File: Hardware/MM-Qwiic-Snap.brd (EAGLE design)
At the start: 67.3 x 58.4 mm, 44 parts, among them J15 MICROMOD-2222-C, J2 QWIIC_RIGHT_ANGLE, U5 AP7361C-33FGEUDFN-8

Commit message: Preliminary schematic done?
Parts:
- added C3, C4: 4.7uF, SparkFun-Capacitors:0603
- added D3: 3A/10V/280mV, SparkFun-DiscreteSemi:SOD-323
- added D4: Yellow, SparkFun-LED:LED-0603
- added JP1: JUMPER-SMT_2_NC_TRACE_SILK, SparkFun-Jumpers:SMT-JUMPER_2_NC_TRACE_SILK
- added R1: 2.2k, SparkFun-Resistors:0603
- added R4: 1k, SparkFun-Resistors:0603
- added U1: MCP73831, SparkFun-IC-Power:SOT23-5
- moved C11 81.3 mm to (-0.85, -138.4)
- moved C10 69.7 mm to (-0.85, -125.7)
- moved C9 59.2 mm to (-0.85, -113.0)
- moved C1 47.6 mm to (-0.85, -100.3)
- moved C13 31.1 mm to (-0.85, -87.6)
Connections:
- new net 5V: C4.1, D3.C, D4.A, JP1.2, U1.4
- new net N$2: R1.2, U1.5
- new net N$3: R4.1, U1.1
- new net N$5: C3.1, D3.A, J3.2, U1.3
- new net N$8: D4.C, R4.2
- net GND: now also C3.2, C4.2, J3.1, R1.1, U1.2
- net VIN: now also JP1.1

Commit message: Board layout
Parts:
- moved R4 180.2 mm to (17.8, 17.8), turned to 270 degrees
- moved JP1 179.6 mm to (15.2, 17.8), flipped to the bottom
- moved D3 176.9 mm to (15.2, 22.9)
- moved D4 173.7 mm to (16.5, 15.2)
- moved C3 170.0 mm to (17.8, 22.9), turned to 90 degrees
- moved C4 168.2 mm to (15.2, 17.8)
- moved C11 147.4 mm to (11.4, 8.47), turned to 270 degrees
- moved C10 134.7 mm to (10.2, 8.47), turned to 270 degrees
- moved C9 121.9 mm to (8.89, 8.47), turned to 270 degrees
- moved C1 117.4 mm to (10.6, 16.5)
- moved C13 106.0 mm to (10.6, 17.8)
- moved R1 101.7 mm to (12.7, 20.3), turned to 270 degrees
- moved U1 96.7 mm to (15.2, 20.3), turned to 90 degrees
- moved BYP 94.6 mm to (3.81, 21.6), flipped to the bottom, turned to 180 degrees
- moved F2 90.3 mm to (3.81, 21.6)
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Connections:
- net 3.3V_EN: now also J15.4
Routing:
- net V_USB: track 0.00 -> 18.9 mm, vias 0 -> 1
- net N$5: track 0.00 -> 12.1 mm
- net VIN: track 0.00 -> 10.7 mm
- net 3.3V: track 0.00 -> 9.96 mm
- net N$1: track 0.00 -> 7.91 mm
- net 5V: track 0.00 -> 7.60 mm, vias 0 -> 1
- net GND: track 0.00 -> 5.90 mm
- net USB_D-: track 0.00 -> 2.58 mm
- net N$4: track 0.00 -> 2.44 mm, vias 0 -> 1
- net USB_D+: track 0.00 -> 2.41 mm
- net N$3: track 0.00 -> 1.87 mm
- net N$8: track 0.00 -> 1.85 mm
- net N$10: track 0.00 -> 1.79 mm
- net N$11: track 0.00 -> 1.63 mm
- net N$2: track 0.00 -> 1.28 mm
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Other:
- board size 67.3 x 58.4 mm -> 78.7 x 34.3 mm

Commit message: Layout
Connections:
- net VIN: now also J15.9
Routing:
- net 3.3V: track 9.96 -> 72.0 mm, vias 0 -> 2
- net VIN: track 10.7 -> 39.8 mm, vias 0 -> 2
- net I2C_SDA: track 0.00 -> 20.2 mm, vias 0 -> 2
- net I2C_SCL: track 0.00 -> 19.6 mm, vias 0 -> 2
- net !RESET!: track 0.00 -> 18.9 mm, vias 0 -> 2
- net 3.3V_EN: track 0.00 -> 17.6 mm, vias 0 -> 1
- net USB_D-: track 2.58 -> 18.9 mm, vias 0 -> 2
- net USB_D+: track 2.41 -> 17.7 mm, vias 0 -> 2
- net !BOOT!: track 0.00 -> 13.9 mm
- net VREG_EN: track 0.00 -> 6.73 mm, vias 0 -> 1
- net 5V: track 7.60 -> 12.0 mm
- net N$1: track 7.91 -> 9.27 mm
- net V_USB: track 18.9 -> 18.3 mm
- net GND: vias 0 -> 10

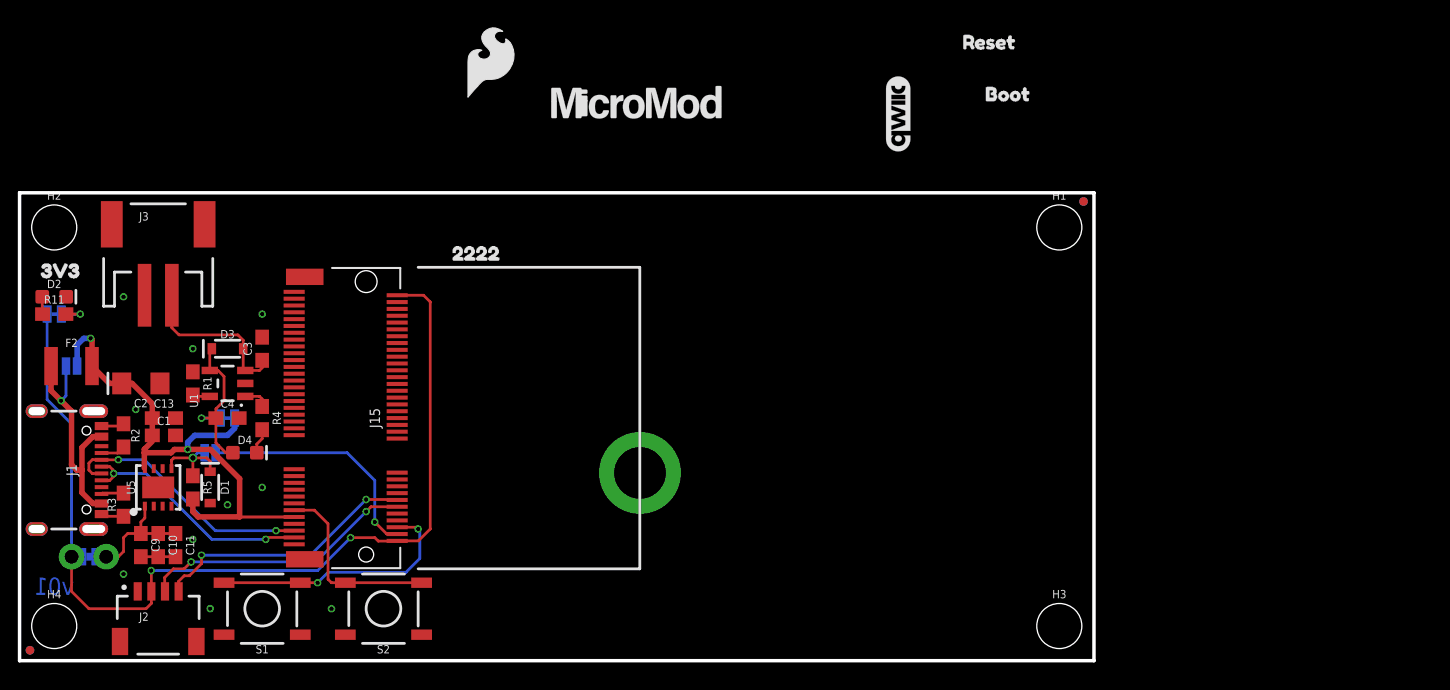
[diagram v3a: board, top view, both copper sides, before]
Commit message: Created part for stand off, proto layout finished
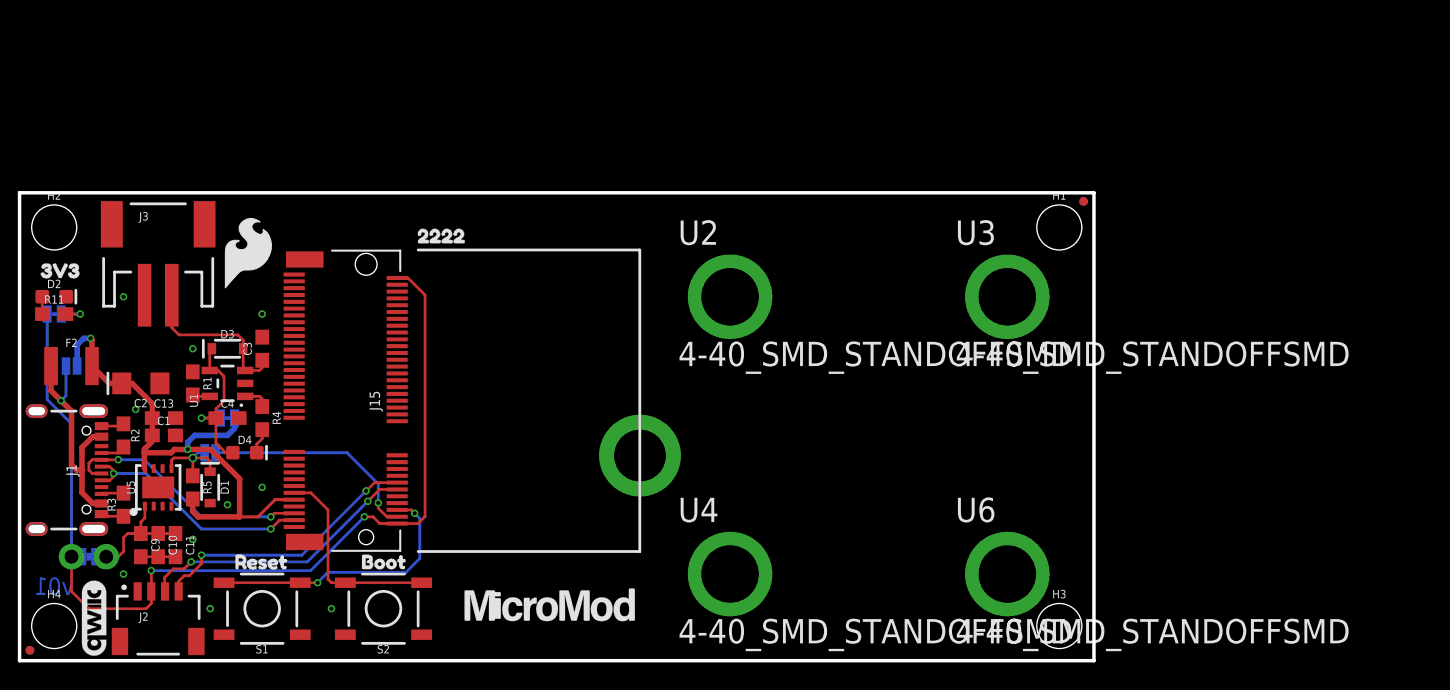
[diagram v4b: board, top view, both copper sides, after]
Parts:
- added U2, U3, U4, U6: 4-40_SMD_STANDOFFSMD, qwiic_carrier:4-40_1/8_SMD_STANDOFF
- moved LOGO2 69.6 mm to (5.46, 3.11)
- moved U$2 65.5 mm to (14.9, 7.24)
- moved U$19 57.1 mm to (24.1, 7.24)
- moved LOGO3 47.7 mm to (24.0, 9.65)
- moved U$68 47.7 mm to (24.1, 15.2)
- moved LOGO1 45.8 mm to (24.1, 19.1)
- moved U$67 37.4 mm to (38.9, 4.06)
- moved U$44 22.6 mm to (16.8, 29.8)
- moved U$55 2.84 mm to (28.2, 31.1)
- moved H5 1.27 mm to (45.5, 15.0)
- moved J15 1.27 mm to (25.4, 19.1)
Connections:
- net GND: now also U2.1, U3.1, U4.1, U6.1
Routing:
- net 3.3V_EN: track 17.6 -> 16.3 mm
- net !BOOT!: track 13.9 -> 15.0 mm
- net !RESET!: track 18.9 -> 19.9 mm
- net I2C_SDA: track 20.2 -> 20.7 mm
- net VIN: track 39.8 -> 40.3 mm
- net I2C_SCL: track 19.6 -> 20.1 mm

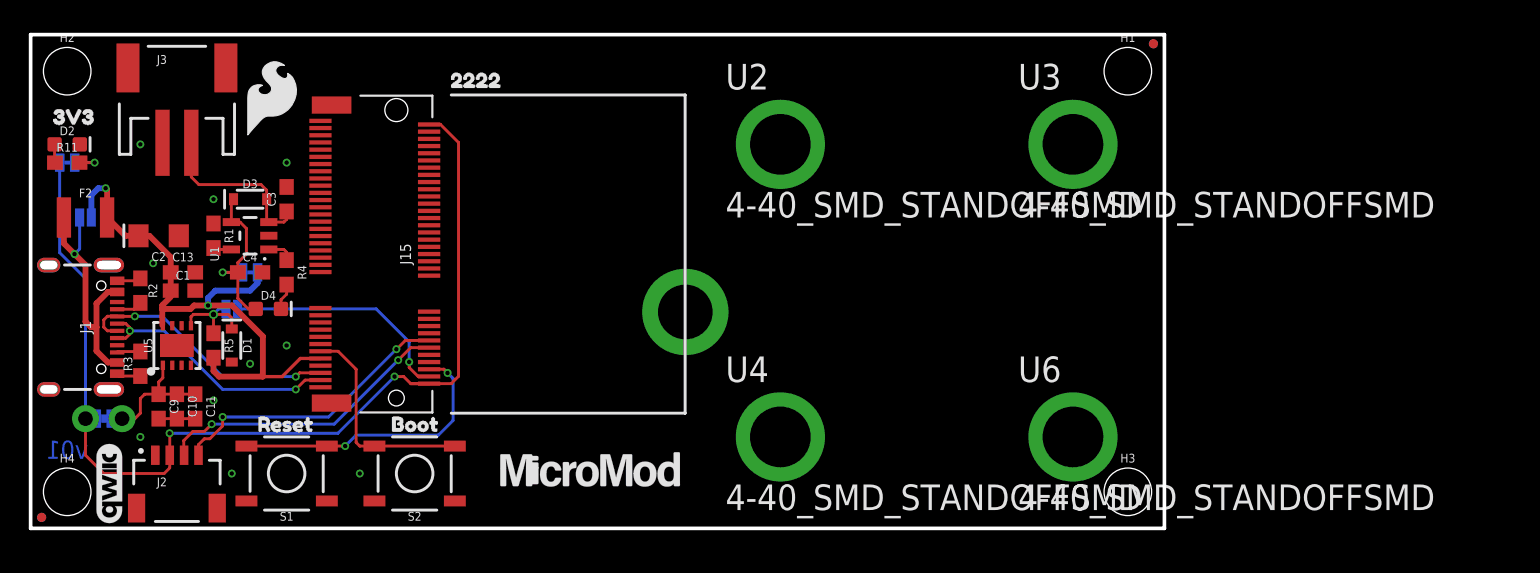
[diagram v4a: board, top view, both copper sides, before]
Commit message: Update MM-Qwiic-Snap.brd
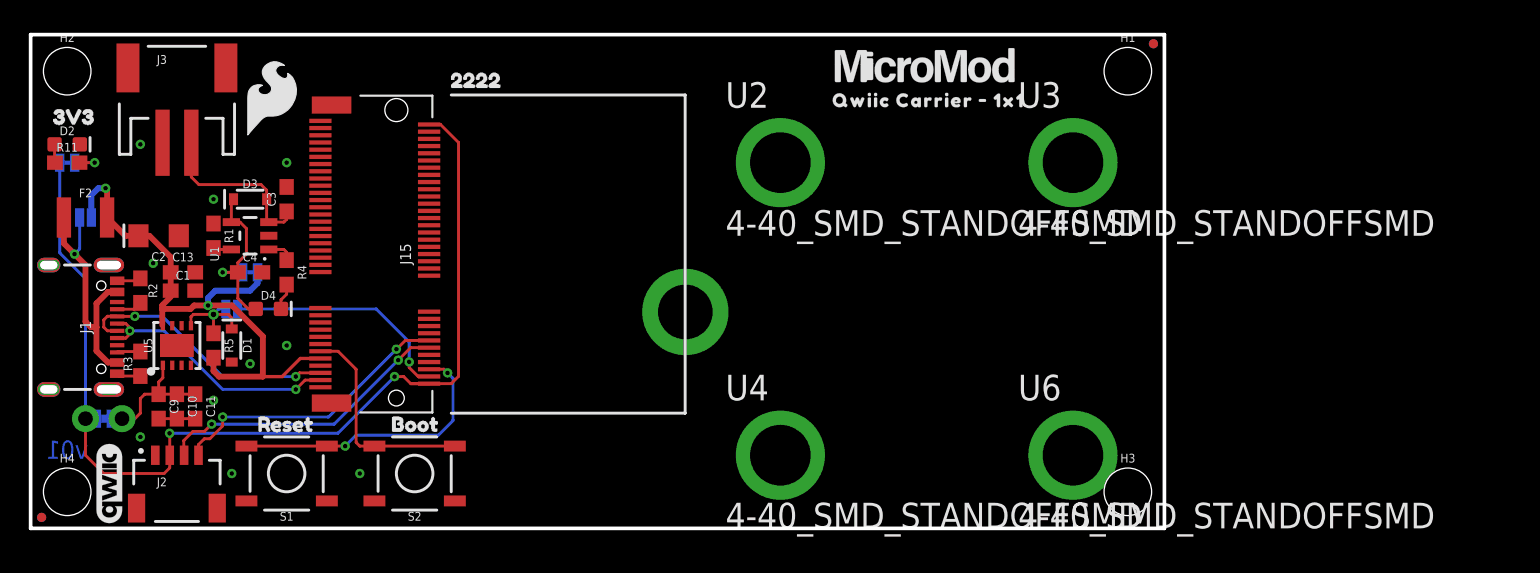
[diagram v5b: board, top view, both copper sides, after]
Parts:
- added U$3: (no value), output:QWIIC_CARRIER_#_1X1_0
- moved U$67 36.4 mm to (62.1, 32.1)
- moved U2 1.27 mm to (52.1, 25.4)
- moved U3 1.27 mm to (72.4, 25.4)
- moved U4 1.27 mm to (52.1, 5.08)
- moved U6 1.27 mm to (72.4, 5.08)
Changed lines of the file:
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@@
 <?xml version="1.0" encoding="utf-8"?>
 <!DOCTYPE eagle SYSTEM "eagle.dtd">
-<eagle version="9.5.2">
+<eagle version="9.6.2">
 <drawing>
 <settings>
-<setting alwaysvectorfont="yes"/>
+<setting alwaysvectorfont="no"/>
 <setting verticaltext="up"/>
 </settings>
@@
 </class>
 </classes>
-<designrules name="SparkFun-2-layer-FAB-LIMIT">
+<designrules name="SparkFun-2-layer-TIGHT">
 <description language="en">&lt;b&gt;SparkFun 2 Layer Design Rule Checks - STANDARD/TIGHT/FAB-LIMIT&lt;/b&gt;
 &lt;p&gt;
@@
 <param name="mtCopper" value="0.035mm 0.035mm 0.035mm 0.035mm 0.035mm 0.035mm 0.035mm 0.035mm 0.035mm 0.035mm 0.035mm 0.035mm 0.035mm 0.035mm 0.035mm 0.035mm"/>
 <param name="mtIsolate" value="1.5mm 0.15mm 0.2mm 0.15mm 0.2mm 0.15mm 0.2mm 0.15mm 0.2mm 0.15mm 0.2mm 0.15mm 0.2mm 0.15mm 0.2mm"/>
-<param name="mdWireWire" value="4mil"/>
-<param name="mdWirePad" value="4mil"/>
-<param name="mdWireVia" value="4mil"/>
-<param name="mdPadPad" value="4mil"/>
-<param name="mdPadVia" value="4mil"/>
-<param name="mdViaVia" value="4mil"/>
-<param name="mdSmdPad" value="4mil"/>
-<param name="mdSmdVia" value="4mil"/>
-<param name="mdSmdSmd" value="4mil"/>
+<param name="mdWireWire" value="7mil"/>
+<param name="mdWirePad" value="7mil"/>
+<param name="mdWireVia" value="7mil"/>
+<param name="mdPadPad" value="7mil"/>
+<param name="mdPadVia" value="7mil"/>
+<param name="mdViaVia" value="7mil"/>
+<param name="mdSmdPad" value="7mil"/>
+<param name="mdSmdVia" value="7mil"/>
+<param name="mdSmdSmd" value="7mil"/>
 <param name="mdViaViaSameLayer" value="8mil"/>
 <param name="mnLayersViaInSmd" value="2"/>
-<param name="mdCopperDimension" value="4mil"/>
-<param name="mdDrill" value="4mil"/>
+<param name="mdCopperDimension" value="7mil"/>
+<param name="mdDrill" value="7mil"/>
 <param name="mdSmdStop" value="0mil"/>
-<param name="msWidth" value="4mil"/>
-<param name="msDrill" value="6mil"/>
+<param name="msWidth" value="7mil"/>
+<param name="msDrill" value="15mil"/>
 <param name="msMicroVia" value="9.99mm"/>
 <param name="msBlindViaRatio" value="0.5"/>
@@
 <param name="rvMicroViaOuter" value="0.25"/>
 <param name="rvMicroViaInner" value="0.25"/>
-<param name="rlMinPadTop" value="5mil"/>
+<param name="rlMinPadTop" value="7mil"/>
 <param name="rlMaxPadTop" value="20mil"/>
-<param name="rlMinPadInner" value="6mil"/>
+<param name="rlMinPadInner" value="7mil"/>
 <param name="rlMaxPadInner" value="20mil"/>
-<param name="rlMinPadBottom" value="5mil"/>
+<param name="rlMinPadBottom" value="7mil"/>
 <param name="rlMaxPadBottom" value="20mil"/>
-<param name="rlMinViaOuter" value="5mil"/>
+<param name="rlMinViaOuter" value="7mil"/>
 <param name="rlMaxViaOuter" value="20mil"/>
-<param name="rlMinViaInner" value="6mil"/>
+<param name="rlMinViaInner" value="7mil"/>
 <param name="rlMaxViaInner" value="20mil"/>
 <param name="rlMinMicroViaOuter" value="4mil"/>
@@
 <element name="U$1" library="buzzard_labels (5)" package="3V31" value="" x="0.635" y="28.575" smashed="yes"/>
 <element name="U$44" library="SparkFun-Aesthetics" package="SFE_LOGO_FLAME_.2" value="" x="16.764" y="29.845" smashed="yes"/>
-<element name="U$67" library="SparkFun-MicroMod" package="MICROMOD_LOGO_.5" value="" x="38.862" y="4.064" smashed="yes"/>
+<element name="U$67" library="SparkFun-MicroMod" package="MICROMOD_LOGO_.5" value="" x="62.103" y="32.131" smashed="yes"/>
 <element name="U$68" library="SparkFun-MicroMod" package="MICROMOD_LOGO_.5" value="" x="24.13" y="15.24" smashed="yes" rot="MR0"/>
 <element name="J2" library="SparkFun-Connectors" package="JST04_1MM_RA" value="QWIIC_RIGHT_ANGLE" x="10.16" y="5.08" smashed="yes">
@@
 <attribute name="VALUE" x="15.24" y="16.637" size="0.6096" layer="28" font="vector" ratio="20" rot="MR0" align="top-center"/>
 </element>
-<element name="U2" library="qwiic_carrier" package="4-40_1/8_SMD_STANDOFF" value="4-40_SMD_STANDOFFSMD" x="52.07" y="26.67" smashed="yes">
-<attribute name="NAME" x="48.26" y="30.48" size="1.778" layer="25"/>
-<attribute name="VALUE" x="48.26" y="21.59" size="1.778" layer="25"/>
-</element>
-<element name="U3" library="qwiic_carrier" package="4-40_1/8_SMD_STANDOFF" value="4-40_SMD_STANDOFFSMD" x="72.39" y="26.67" smashed="yes">
-<attribute name="NAME" x="68.58" y="30.48" size="1.778" layer="25"/>
-<attribute name="VALUE" x="68.58" y="21.59" size="1.778" layer="25"/>
-</element>
-<element name="U4" library="qwiic_carrier" package="4-40_1/8_SMD_STANDOFF" value="4-40_SMD_STANDOFFSMD" x="52.07" y="6.35" smashed="yes">
-<attribute name="NAME" x="48.26" y="10.16" size="1.778" layer="25"/>
-<attribute name="VALUE" x="48.26" y="1.27" size="1.778" layer="25"/>
-</element>
-<element name="U6" library="qwiic_carrier" package="4-40_1/8_SMD_STANDOFF" value="4-40_SMD_STANDOFFSMD" x="72.39" y="6.35" smashed="yes">
-<attribute name="NAME" x="68.58" y="10.16" size="1.778" layer="25"/>
-<attribute name="VALUE" x="68.58" y="1.27" size="1.778" layer="25"/>
-</element>
+<element name="U2" library="qwiic_carrier" package="4-40_1/8_SMD_STANDOFF" value="4-40_SMD_STANDOFFSMD" x="52.07" y="25.4" smashed="yes">
+<attribute name="NAME" x="48.26" y="29.21" size="1.778" layer="25"/>
+<attribute name="VALUE" x="48.26" y="20.32" size="1.778" layer="25"/>
+</element>
+<element name="U3" library="qwiic_carrier" package="4-40_1/8_SMD_STANDOFF" value="4-40_SMD_STANDOFFSMD" x="72.39" y="25.4" smashed="yes">
+<attribute name="NAME" x="68.58" y="29.21" size="1.778" layer="25"/>
+<attribute name="VALUE" x="68.58" y="20.32" size="1.778" layer="25"/>
+</element>
+<element name="U4" library="qwiic_carrier" package="4-40_1/8_SMD_STANDOFF" value="4-40_SMD_STANDOFFSMD" x="52.07" y="5.08" smashed="yes">
+<attribute name="NAME" x="48.26" y="8.89" size="1.778" layer="25"/>
+<attribute name="VALUE" x="48.26" y="0" size="1.778" layer="25"/>
+</element>
+<element name="U6" library="qwiic_carrier" package="4-40_1/8_SMD_STANDOFF" value="4-40_SMD_STANDOFFSMD" x="72.39" y="5.08" smashed="yes">
+<attribute name="NAME" x="68.58" y="8.89" size="1.778" layer="25"/>
+<attribute name="VALUE" x="68.58" y="0" size="1.778" layer="25"/>
+</element>
+<element name="U$3" library="output" package="QWIIC_CARRIER_#_1X1_0" value="" x="54.991" y="29.718" smashed="yes"/>
 </elements>
 <signals>
@@
 <mfgpreviewcolor name="substratecolor" color="0xFF786E46"/>
 </mfgpreviewcolors>
+<errors>
+</errors>
 </board>
 </drawing>

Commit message: Switch out stand offs
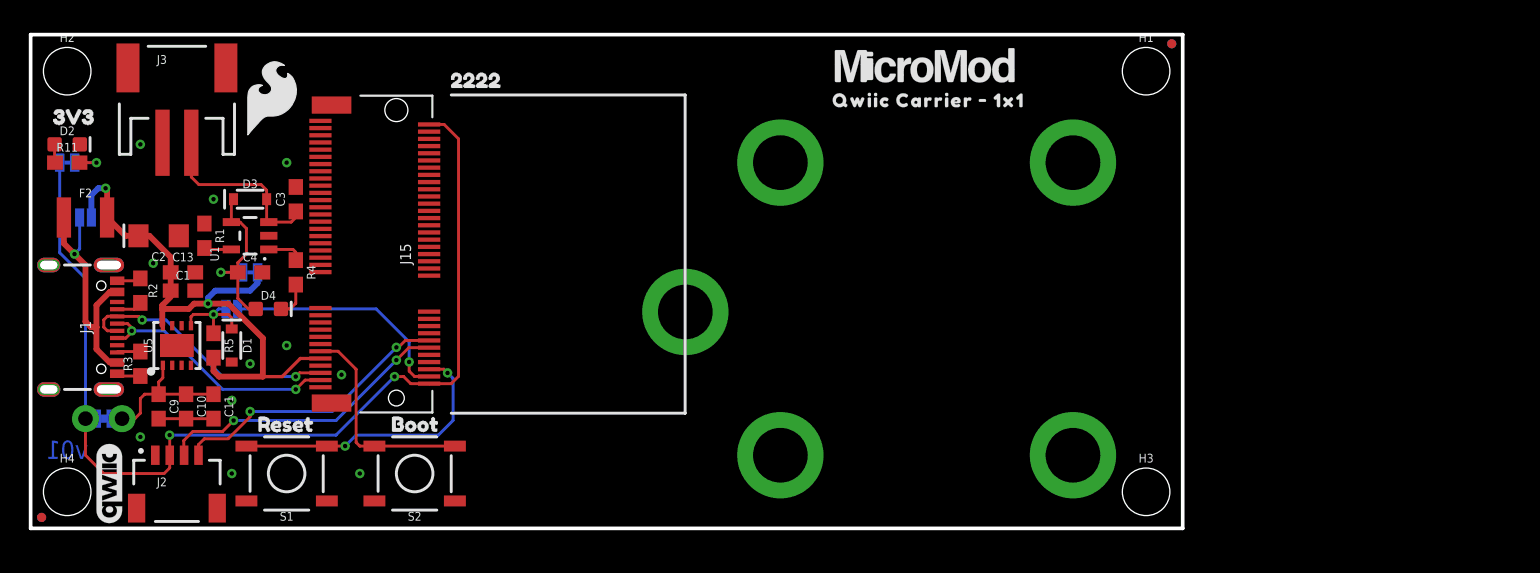
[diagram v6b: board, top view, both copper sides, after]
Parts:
- removed U2, U3, U4, U6: 4-40_SMD_STANDOFFSMD, qwiic_carrier:4-40_1/8_SMD_STANDOFF
- added H6, H7, H8, H9: STAND-OFF-REFLOW2.5MM_TALL, SparkFun-Hardware:STAND-OFF-REFLOW-M2.5
- moved FD2 1.27 mm to (79.2, 33.7)
- moved FD4 1.27 mm to (79.2, 33.7)
- moved C11 1.27 mm to (12.7, 8.47)
- moved H1 1.27 mm to (77.5, 31.8)
- moved H3 1.27 mm to (77.5, 2.54)
- moved C10 0.63 mm to (10.8, 8.47)
- moved R1 0.63 mm to (12.1, 20.3)
- moved C3 0.63 mm to (18.4, 22.9)
- moved R4 0.63 mm to (18.4, 17.8)
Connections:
- net GND: now also H6.1, H7.1, H8.1, H9.1; no longer U2.1, U3.1, U4.1, U6.1
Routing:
- net GND: track 5.90 -> 7.17 mm, vias 10 -> 11
- net N$1: track 9.27 -> 10.5 mm
- net N$2: track 1.28 -> 1.92 mm
- net N$3: track 1.87 -> 2.50 mm
- net N$8: track 1.85 -> 2.49 mm
- net N$5: track 12.1 -> 12.7 mm
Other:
- board size 78.7 x 34.3 mm -> 80 x 34.3 mm
